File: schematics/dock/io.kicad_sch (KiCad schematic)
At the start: 6 parts, among them U1 TM1637

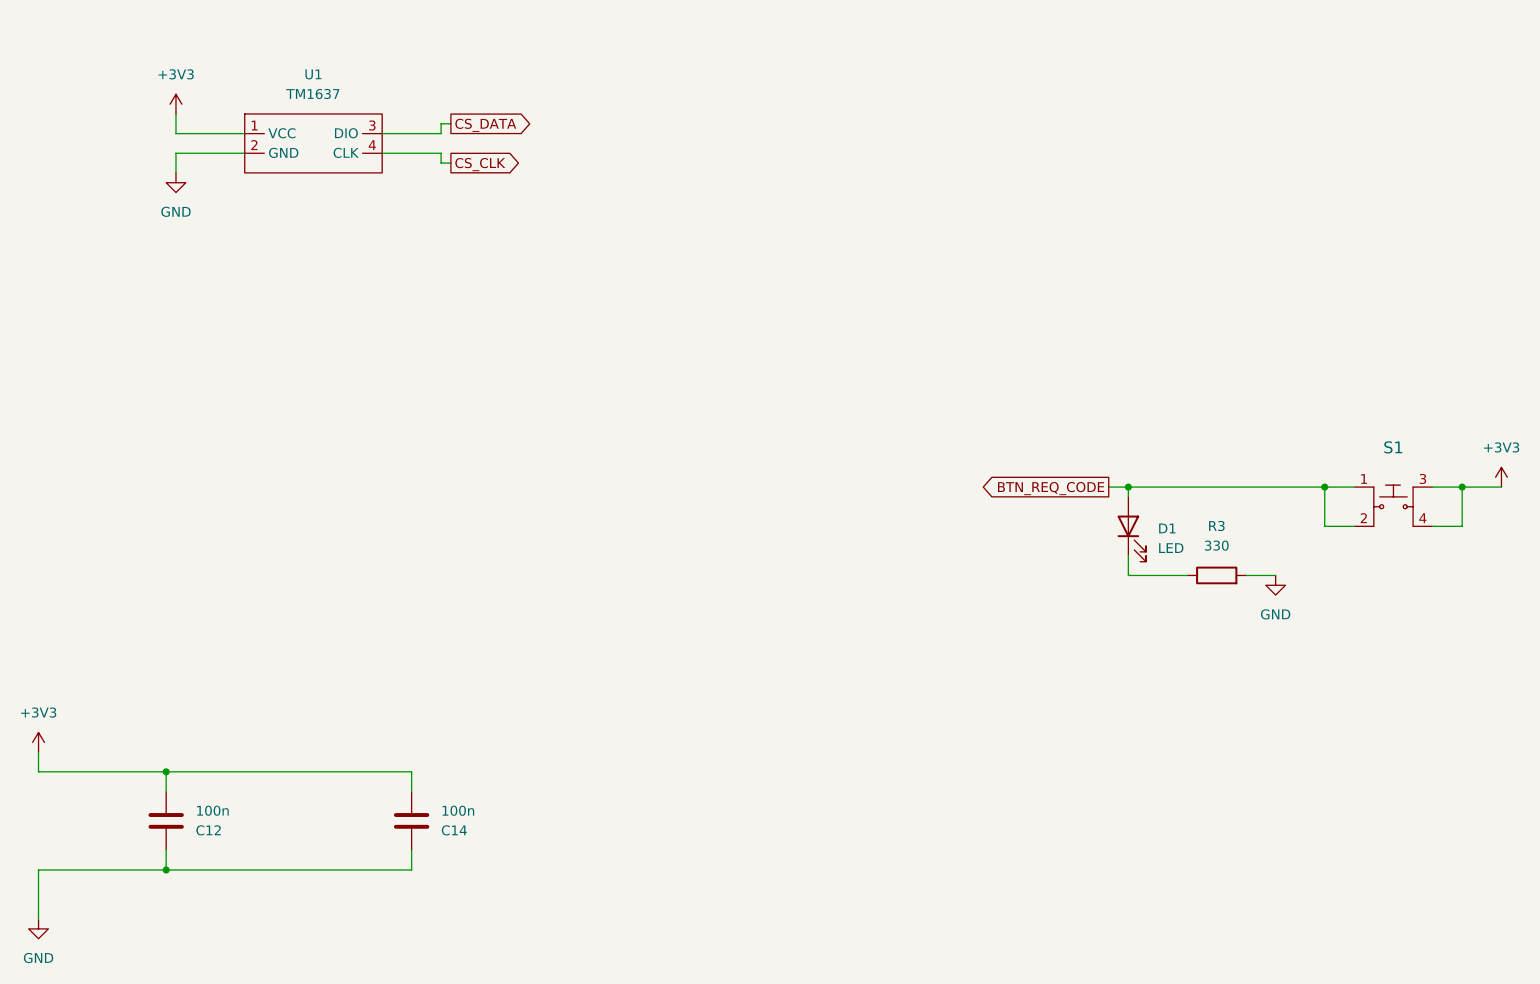
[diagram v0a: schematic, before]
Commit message: Added various tests, started work on off-board controller
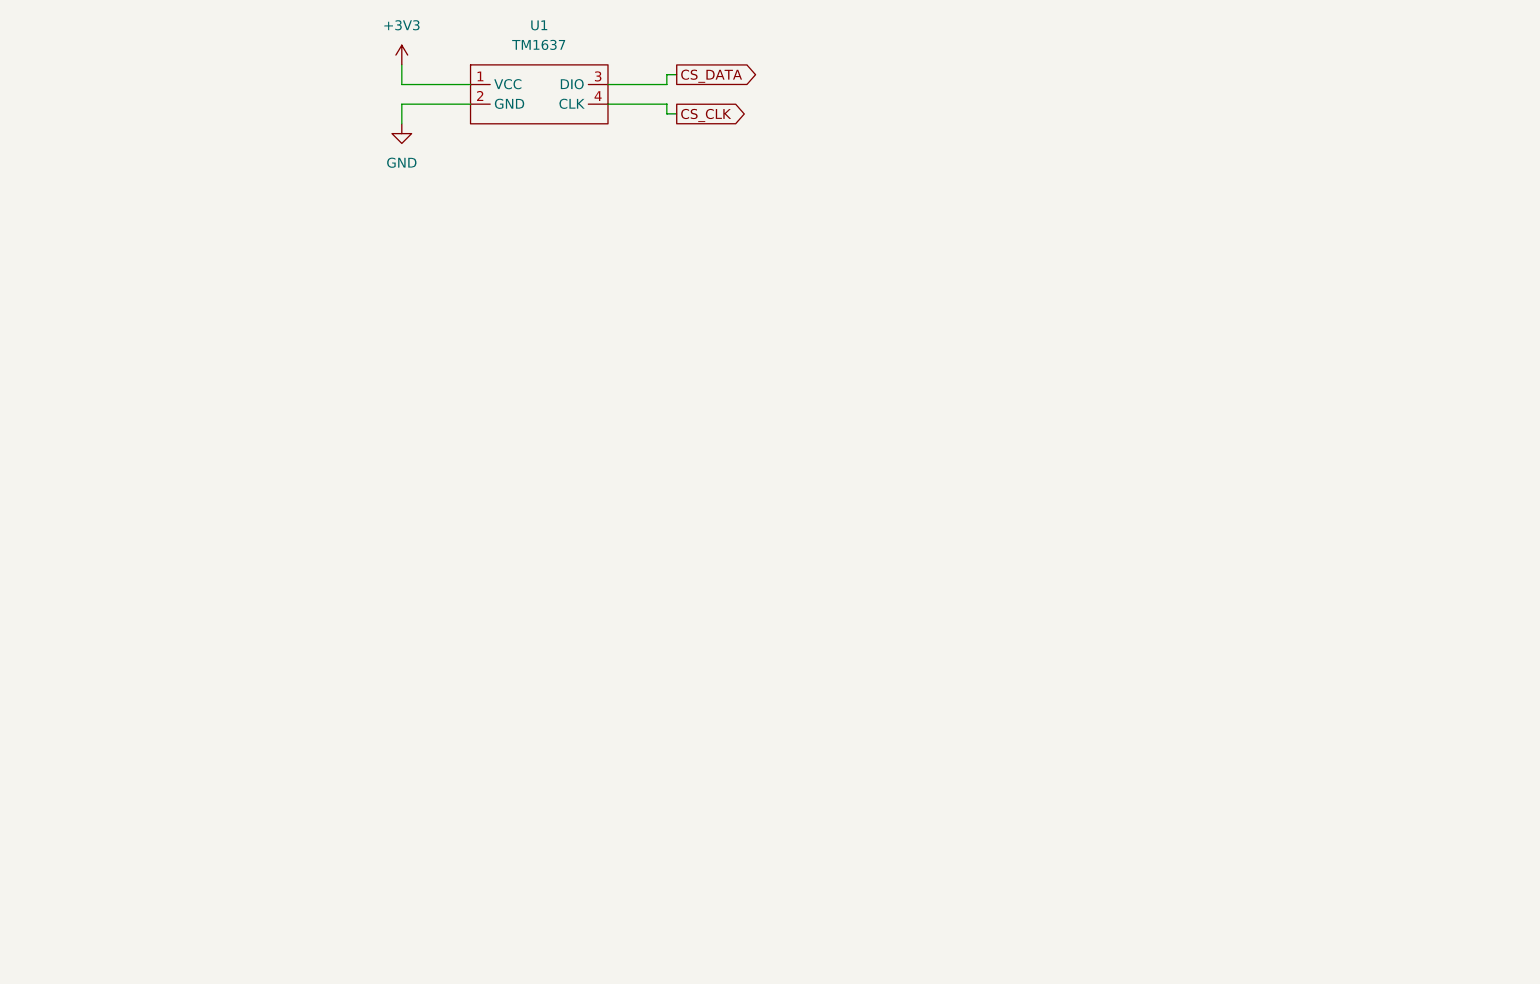
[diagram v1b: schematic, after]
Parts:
- removed C12, C14: 100n, Capacitor_SMD:C_0805_2012Metric_Pad1.18x1.45mm_HandSolder, symbol Device:C
- removed D1: LED, LED_SMD:LED_0805_2012Metric_Pad1.15x1.40mm_HandSolder, symbol Device:LED
- removed R3: 330, Resistor_SMD:R_0805_2012Metric_Pad1.20x1.40mm_HandSolder, symbol Device:R
- removed S1: ~, sub:button, symbol dk_Tactile-Switches:1825910-6
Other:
- moved on the sheet: U1

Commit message: Added dock code
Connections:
- net CS_CLK renamed DISPLAY_CLK
- net CS_DATA renamed DISPLAY_DATA
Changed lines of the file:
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@@
 		)
 	)
-	(global_label "CS_CLK"
+	(global_label "DISPLAY_CLK"
 		(shape output)
 		(at 166.37 83.82 0)
@@
 		)
 	)
-	(global_label "CS_DATA"
+	(global_label "DISPLAY_DATA"
 		(shape output)
 		(at 166.37 78.74 0)
